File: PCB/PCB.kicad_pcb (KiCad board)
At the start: 4 copper layers, 85 x 56 mm, 22 parts, among them J10 Mot2, J11 UBEC, J12 Spare_GPIO_Conn, J4 Servo_Conn_4, J5 Servo_Conn_5, J6 Servo_Conn_6, J7 Mot1_Conn, J8 Mot2_Conn, J9 Mot1

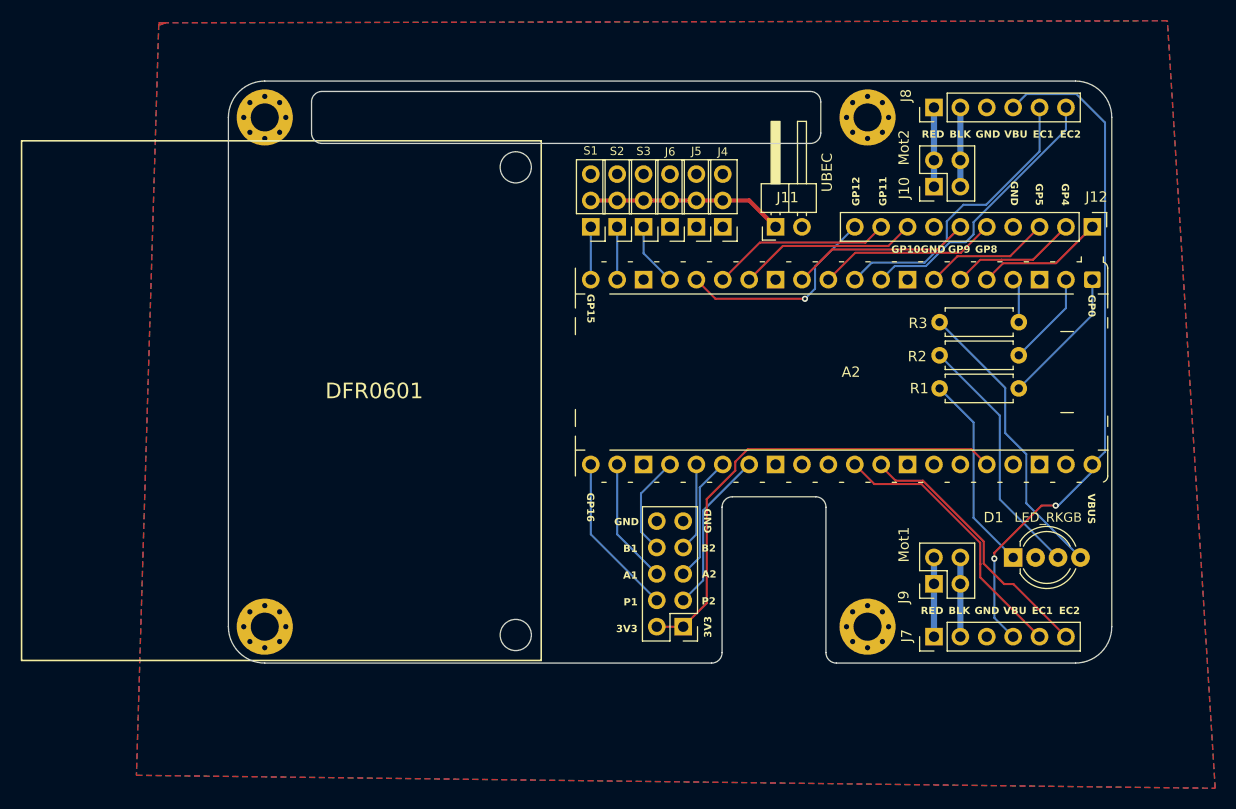
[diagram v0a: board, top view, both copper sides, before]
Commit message: update PCB labeling and gerber
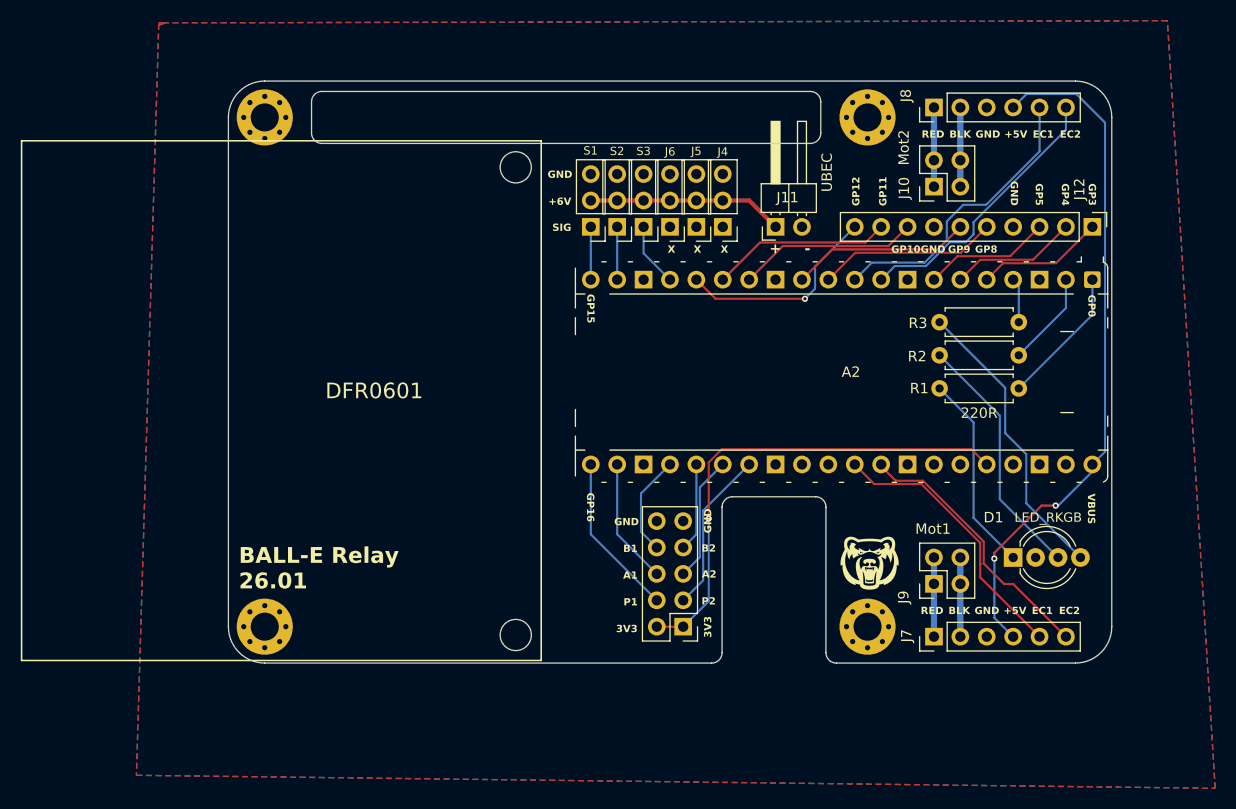
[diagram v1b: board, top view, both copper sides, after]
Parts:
- added G***: LOGO, LOGO, F.Cu at (111.7, 96.9)
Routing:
- net +3V3: track 45.8 -> 47.3 mm, vias 0 -> 1
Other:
- board text added: "+"
- board text added: "+5V"
- board text added: "+6V"
- board text added: "-"
- board text added: "BALL-E Relay 26.01"
- board text added: "GP3"
- board text added: "SIG"
- board text added: "X"
- board text removed: "VBU"
